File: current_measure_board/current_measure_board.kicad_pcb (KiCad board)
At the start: 6 copper layers, 76.2 x 76.2 mm, 39 parts, among them U1 LT6370HMS8-TRPBF, U2 LT1793AIS8-PBF, U3 LT1793AIS8-PBF, U4 LT1793AIS8-PBF

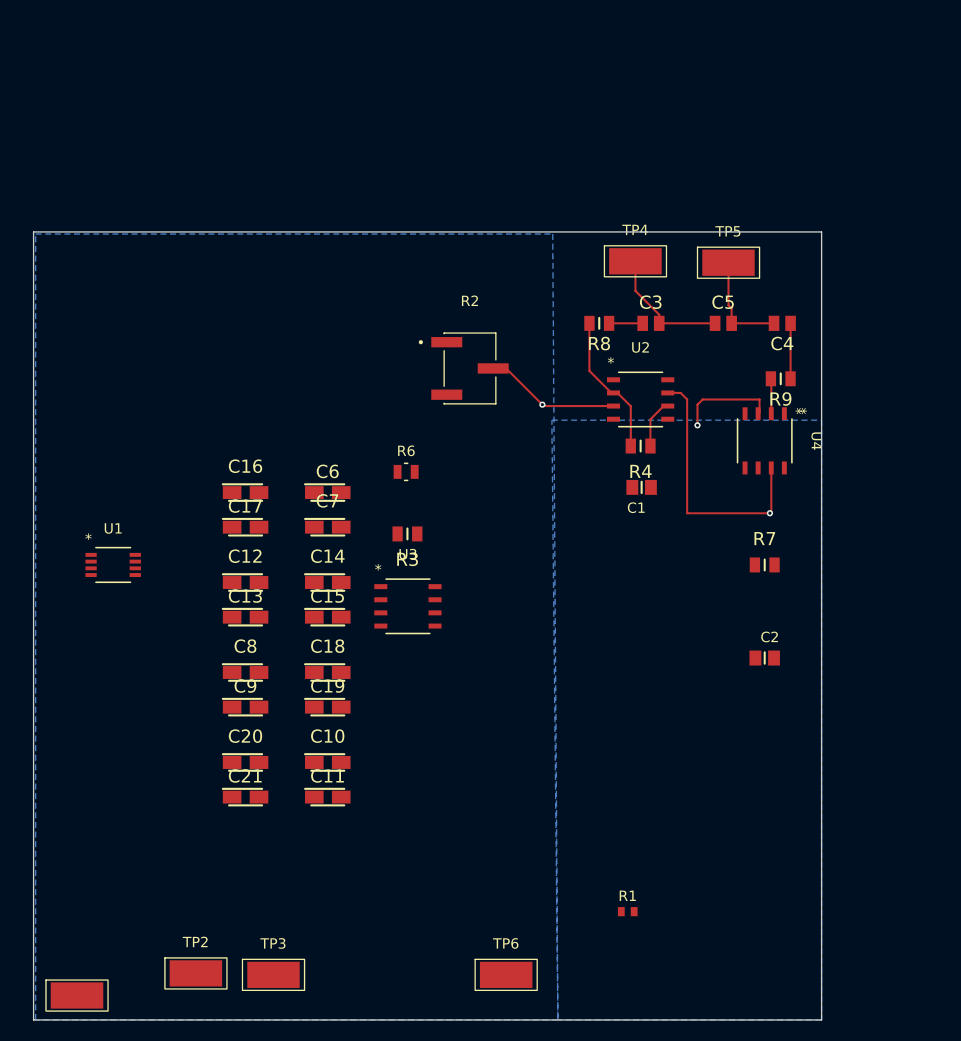
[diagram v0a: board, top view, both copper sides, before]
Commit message: high impedance section draft done
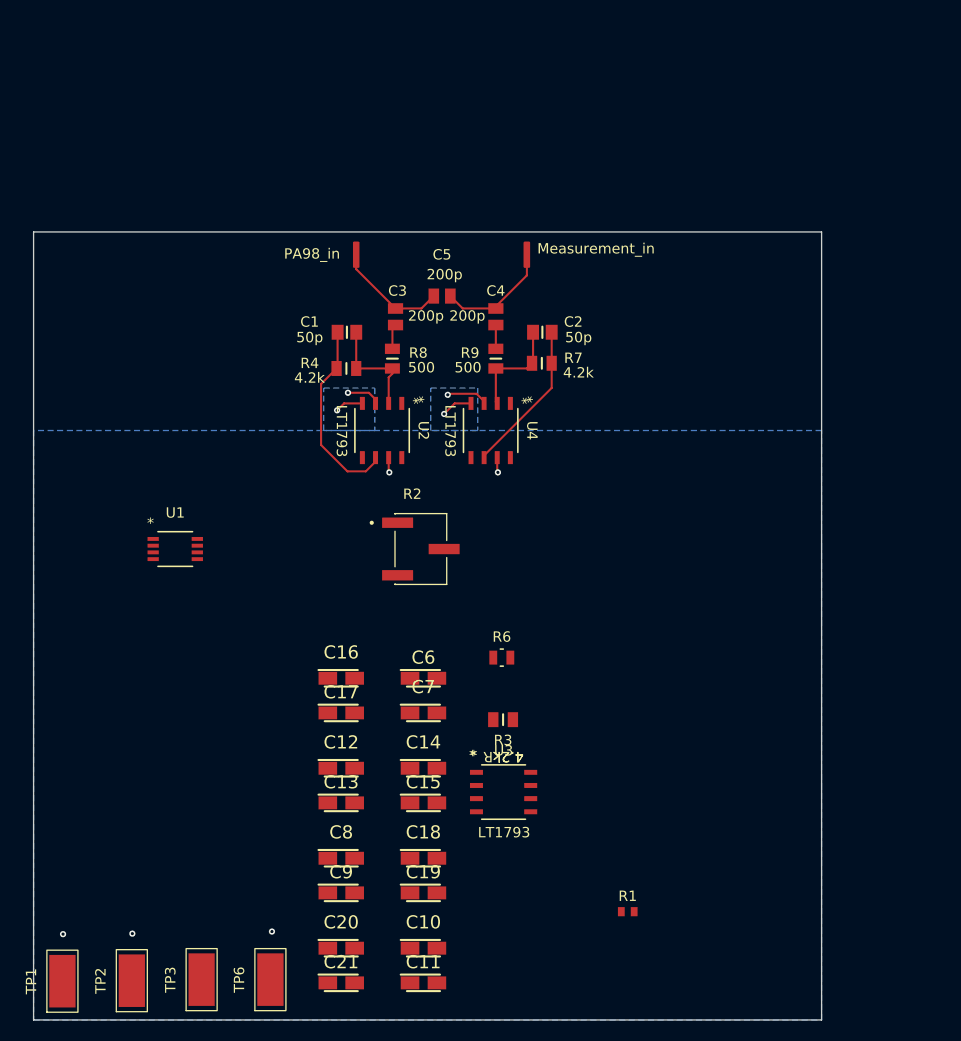
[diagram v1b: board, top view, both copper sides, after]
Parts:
- TP4, TP5: footprint Custom_trimpot:PAD_EXT_2.54x5.08mm -> Custom_testpoint:PAD_EXT_0.635x2.54mm
- moved C2 38.1 mm to (149.5, 85.0), turned to 180 degrees
- moved C1 32.2 mm to (130.6, 85.0), turned to 0 degrees
- moved R4 29.4 mm to (130.6, 88.5), turned to 0 degrees
- moved R7 29.1 mm to (149.4, 88.0), turned to 180 degrees
- moved C4 27.7 mm to (145.0, 83.5), turned to 90 degrees
- moved R9 27.6 mm to (145.0, 87.5), turned to -90 degrees
- moved C5 27.3 mm to (139.8, 81.5)
- moved TP4 27.2 mm to (131.5, 77.5)
- moved U4 26.5 mm to (144.5, 94.5)
- moved U2 25.2 mm to (134.0, 94.5), turned to -90 degrees
- moved C3 24.7 mm to (135.3, 83.5), turned to 90 degrees
- moved TP6 20.4 mm to (125.7, 147.6), turned to 90 degrees
- moved R8 20.3 mm to (135.0, 87.5), turned to -90 degrees
- moved C17 20.2 mm to (130.1, 121.8)
- moved C20 20.2 mm to (130.1, 144.6)
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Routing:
- net /Vplus: track 27.0 -> 2.91 mm, vias 1 -> 3
- net GND: track 22.8 -> 7.38 mm, vias 2 -> 3
- net Net-(U3-+INA): track 0.00 -> 14.8 mm
- net Net-(U1-IN-): track 4.99 -> 18.7 mm
- net Net-(U4--INA): track 3.39 -> 10.2 mm
- net /Vminus: track 0.00 -> 5.74 mm, vias 0 -> 3
- net Net-(U2--INA): track 13.9 -> 10.5 mm
- net Net-(C4-Pad1): track 5.36 -> 2.30 mm
- net /PA98_in: track 12.4 -> 11.0 mm
- net /measurement_in: track 10.1 -> 11.3 mm
- net Net-(C3-Pad1): track 3.25 -> 2.42 mm
- added copper zone on In4.Cu, net /Vminus
- added copper zone on In3.Cu, net /Vplus
- removed copper zone on In1.Cu, net /Vplus
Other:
- board text added: "Measurement_in"
- board text added: "PA98_in"

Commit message: Power buffer done
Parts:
- moved C20 72.8 mm to (169.7, 83.5)
- moved C21 71.6 mm to (169.8, 88.3)
- moved C18 64.7 mm to (176.3, 83.7)
- moved C19 63.7 mm to (176.3, 88.3)
- moved C14 45.1 mm to (124.8, 84.0)
- moved C15 43.7 mm to (125.0, 88.8)
- moved R2 40.6 mm to (178.4, 105.5)
- moved C16 36.4 mm to (118.3, 84.0)
- moved C17 35.1 mm to (118.3, 88.7)
- moved U3 34.4 mm to (168.7, 103.8)
- moved U1 32.0 mm to (140.0, 87.2), turned to -90 degrees
- moved TP3 19.8 mm to (128.3, 130.0)
- moved TP6 19.8 mm to (134.9, 130.0)
- moved C10 19.8 mm to (147.2, 127.0)
- moved C11 19.8 mm to (147.2, 130.3)
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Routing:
- net GND: track 7.38 -> 39.9 mm, vias 3 -> 7
- net /Vplus: track 2.91 -> 20.2 mm, vias 3 -> 5
- net /Vminus: track 5.74 -> 23.0 mm, vias 3 -> 5
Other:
- board text added: "U2 Power Buffer"
- board text added: "U4 Power Buffer"
- board text added: "V+"
- board text added: "V-"

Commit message: Update
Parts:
- added REF**: MountingHole_2.1mm, MountingHole:MountingHole_2.1mm, F.Cu at (112.4, 60.9)
- added REF**: MountingHole_2.1mm, MountingHole:MountingHole_2.1mm, F.Cu at (182.6, 130.9)
- added REF**: MountingHole_2.1mm, MountingHole:MountingHole_2.1mm, F.Cu at (112.4, 130.9)
- added REF**: MountingHole_2.1mm, MountingHole:MountingHole_2.1mm, F.Cu at (182.6, 60.9)
- moved R1 42.7 mm to (128.2, 105.5)
- moved C10 33.1 mm to (117.2, 113.2), turned to 90 degrees
- moved C11 31.2 mm to (121.1, 113.2), turned to 90 degrees
- moved C7 26.5 mm to (171.0, 115.8)
- moved U1 26.4 mm to (128.3, 110.9), turned to 0 degrees
- moved C6 26.1 mm to (171.2, 111.2)
- moved TP1 23.1 mm to (137.9, 130.1)
- moved C17 21.3 mm to (134.7, 75.1), turned to 90 degrees
- moved C21 20.3 mm to (149.4, 88.6)
- moved C20 20.3 mm to (149.4, 83.8)
- moved C9 19.1 mm to (156.2, 112.7), turned to 90 degrees
- moved C18 17.2 mm to (159.2, 84.0)
- moved C19 17.2 mm to (159.2, 88.7)
- moved TP3 17.1 mm to (145.4, 130.2)
- moved C14 16.3 mm to (141.2, 83.9)
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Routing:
- net Net-(U1-IN+): track 0.00 -> 64.2 mm, vias 0 -> 2
- net Net-(U1-IN-): track 18.7 -> 61.8 mm, vias 0 -> 2
- net Net-(U3-+INA): track 14.8 -> 49.2 mm
- net GND: track 39.9 -> 71.5 mm, vias 7 -> 13
- net /Vminus: track 23.0 -> 52.4 mm
- net /Vplus: track 20.2 -> 45.0 mm
- net Net-(U3--INA): track 0.00 -> 23.4 mm
- net Net-(U1-RG+): track 0.00 -> 5.70 mm
- net Net-(U1-RG-): track 0.00 -> 5.59 mm
- net Net-(R2-Pad1): track 0.00 -> 4.75 mm
- net /Control_out: track 0.00 -> 1.69 mm
- added copper zone on In2.Cu, net GND
- removed copper zone on B.Cu, net GND
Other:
- board text added: "Ctrl"
- board text added: "DOuble the width"
- board text added: "GND"
- board text added: "U3 V+"
- board text added: "U3 V-"
- board text removed: "U2 Power Buffer"
- board text removed: "U4 Power Buffer"

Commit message: Update
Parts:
- moved C17 13.5 mm to (127.3, 86.5), turned to 0 degrees
- moved C2 11.7 mm to (169.7, 71.5), turned to 90 degrees
- moved C19 10.7 mm to (168.3, 83.1)
- moved C18 10.7 mm to (168.3, 78.5)
- moved C10 10.3 mm to (123.4, 105.0)
- moved C11 10.3 mm to (127.3, 105.0)
- moved C12 10.3 mm to (141.2, 100.7)
- moved C13 10.3 mm to (145.2, 100.8)
- moved R1 10.3 mm to (134.5, 97.3)
- moved U1 10.3 mm to (134.6, 102.7)
- moved C3 9.43 mm to (135.1, 65.6)
- moved U2 9.38 mm to (134.1, 78.9), turned to 0 degrees
- moved R8 9.17 mm to (135.1, 69.8)
- moved R7 8.05 mm to (166.7, 71.5), turned to 90 degrees
- moved C16 7.25 mm to (127.3, 81.8), turned to 0 degrees
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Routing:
- net /Control_out: track 1.69 -> 30.9 mm
- net Net-(U1-IN-): track 61.8 -> 41.8 mm, vias 2 -> 0
- net GND: track 71.5 -> 84.1 mm
- net Net-(U2--INA): track 10.5 -> 22.4 mm
- net Net-(U4--INA): track 10.2 -> 20.9 mm
- net /Vplus: track 45.0 -> 52.5 mm
- net Net-(U1-IN+): track 64.2 -> 59.2 mm
- net /measurement_in: track 11.3 -> 16.1 mm
- net /PA98_in: track 11.0 -> 15.7 mm
- net Net-(U3-+INA): track 49.2 -> 53.4 mm
- net /Vminus: track 52.4 -> 49.8 mm
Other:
- board text removed: "DOuble the width"
- board text removed: "U3 V+"
- board text removed: "U3 V-"

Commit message: current board update
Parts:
- added C22: C1206C104K5RACTM, Custom_capacitors:CAPPM3216X180N(0.1uF 1206 0.1acc), F.Cu at (182.7, 84.2)
- added C23: TH3A105K035D6600, Custom_capacitors:CAPPM3216X180N(1uF 35V 1206 0.1err, F.Cu at (182.7, 88.1)
- added C24: C1206C104K5RACTM, Custom_capacitors:CAPPM3216X180N(0.1uF 1206 0.1acc), F.Cu at (168.3, 87.7)
- added C25: TH3A105K035D6600, Custom_capacitors:CAPPM3216X180N(1uF 35V 1206 0.1err, F.Cu at (168.4, 90.5)
- added C26: 50p, Custom_capacitors:CAPC2012X140N(50pF 1206 1 C0G 100V), F.Cu at (173.0, 78.0)
- added R10: 4.2k, Custom_resistors:RESC2012X55N(4.02k Ohm 0805 0.1err), F.Cu at (173.0, 75.0)
- added TP10: TestPoint, Custom_testpoint:PAD_EXT_0.635x2.54mm, F.Cu at (169.2, 60.5)
- added TP7: TestPoint, Custom_trimpot:PAD_EXT_2.54x5.08mm, F.Cu at (113.8, 120.7)
- added TP8: TestPoint, Custom_trimpot:PAD_EXT_2.54x5.08mm, F.Cu at (180.9, 101.7)
- added TP9: TestPoint, Custom_trimpot:PAD_EXT_2.54x5.08mm, F.Cu at (180.9, 107.9)
- added U5: LT1793AIS8-PBF, Custom_amplifiers:LT1793AIS_8_PBF, F.Cu at (175.9, 83.5)
- moved TP3 38.3 mm to (113.8, 108.6), turned to 180 degrees
- moved C21 9.91 mm to (143.4, 85.2)
- moved R6 9.91 mm to (157.9, 98.8)
- moved U4 9.91 mm to (150.6, 77.0)
- moved C10 9.91 mm to (113.5, 104.0)
- moved C11 9.91 mm to (117.5, 103.9)
- moved R8 9.91 mm to (125.2, 68.8)
- moved TP4 9.91 mm to (125.3, 60.2)
- moved U1 9.91 mm to (124.7, 101.6)
- moved U2 9.91 mm to (124.2, 77.8)
- moved C1 9.91 mm to (131.6, 70.7)
- moved C12 9.91 mm to (131.4, 99.6)
- moved C13 9.91 mm to (135.3, 99.7)
- moved C14 9.91 mm to (132.2, 78.0)
- moved C15 9.91 mm to (132.3, 82.7)
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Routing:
- net /Current_meas: track 0.00 -> 31.3 mm
- net GND: track 84.1 -> 112.2 mm, vias 13 -> 18
- net /Current_in: track 0.00 -> 24.2 mm
- net /Control_out: track 30.9 -> 16.9 mm
- net /Vplus: track 52.5 -> 64.3 mm, vias 5 -> 6
- net /Vminus: track 49.8 -> 59.9 mm, vias 5 -> 6
- net Net-(U3--INA): track 23.4 -> 13.5 mm
- net Net-(U1-RG+): track 5.70 -> 2.55 mm
- net Net-(U1-RG-): track 5.59 -> 2.80 mm
- net Net-(U3-+INA): track 53.4 -> 50.8 mm
- net Net-(U1-IN-): track 41.8 -> 42.5 mm
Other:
- board text added: "Ctrl_GND"
- board text added: "Current_in"
- board text added: "Current_meas"
